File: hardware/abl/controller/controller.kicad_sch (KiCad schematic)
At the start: 31 parts, among them IC1 LSF0204PWJ, IC2 FXL6408UMX, IC3 VEML6040A3OG, IC4 FXL6408UMX, J1 SFW20S-2STE1LF, J2 Conn_02x03_Odd_Even, J3 Conn_02x03_Odd_Even, J4 PRT-14417, J5 Conn_02x04_Odd_Even, Q2 AO3401A, Q4 AO3401A, U1 INA219AxD

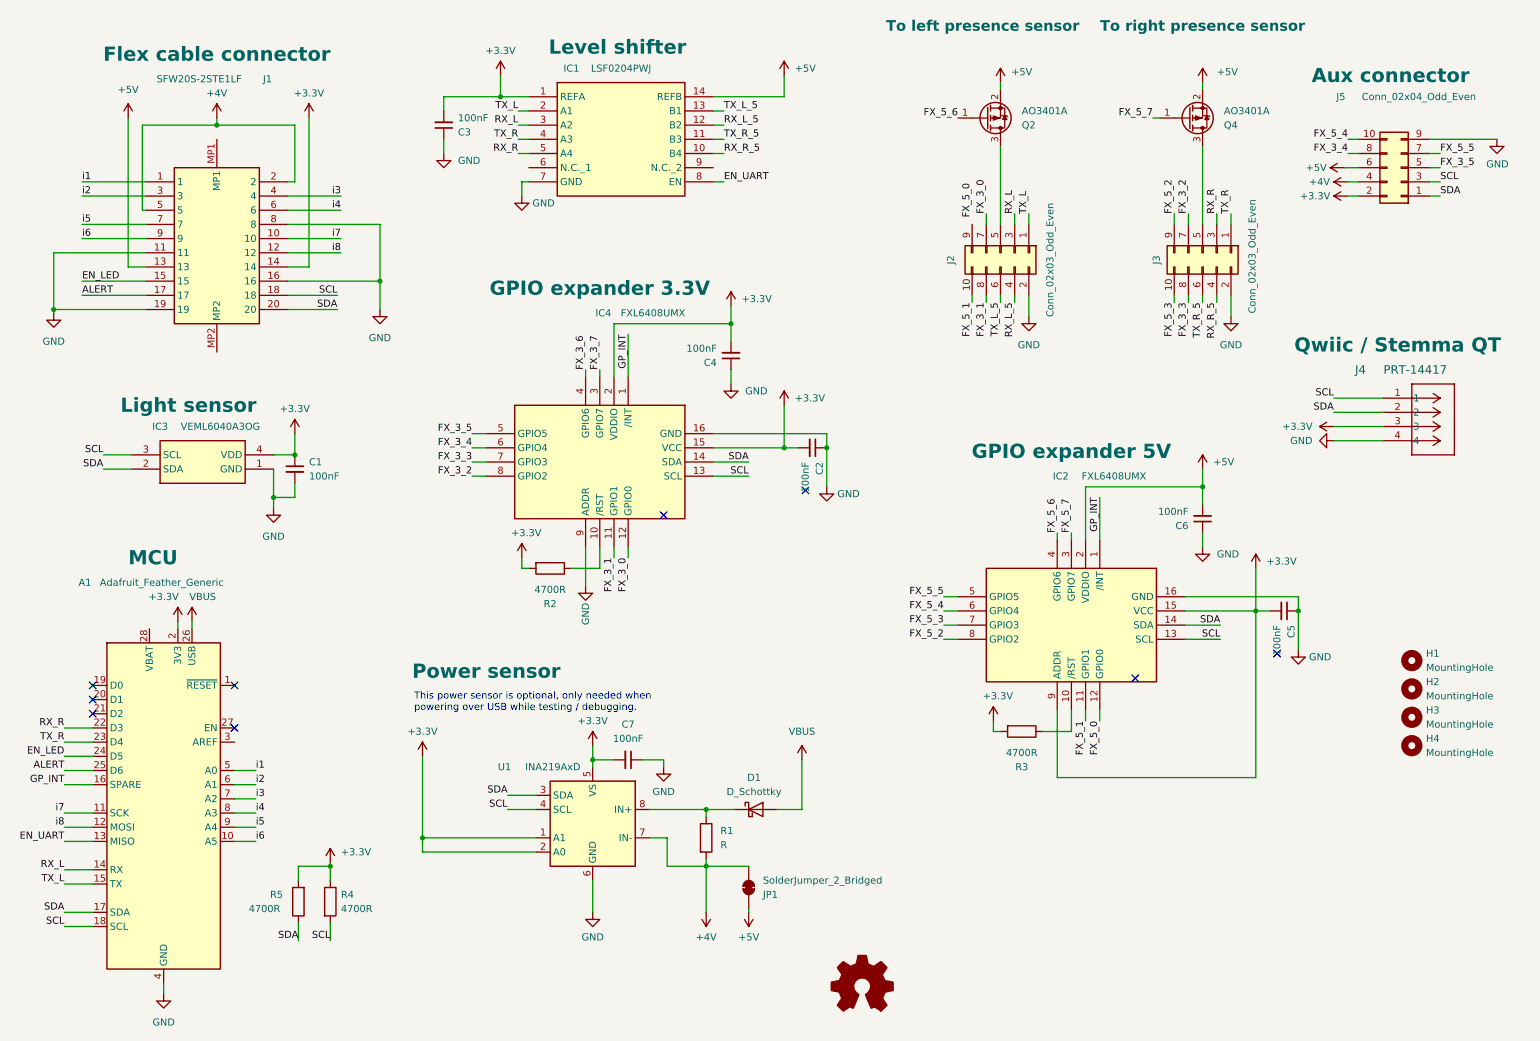
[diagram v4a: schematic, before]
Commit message: Make controller PCB ready for prototype prodution: change level shifter, re-route many traces, etc.
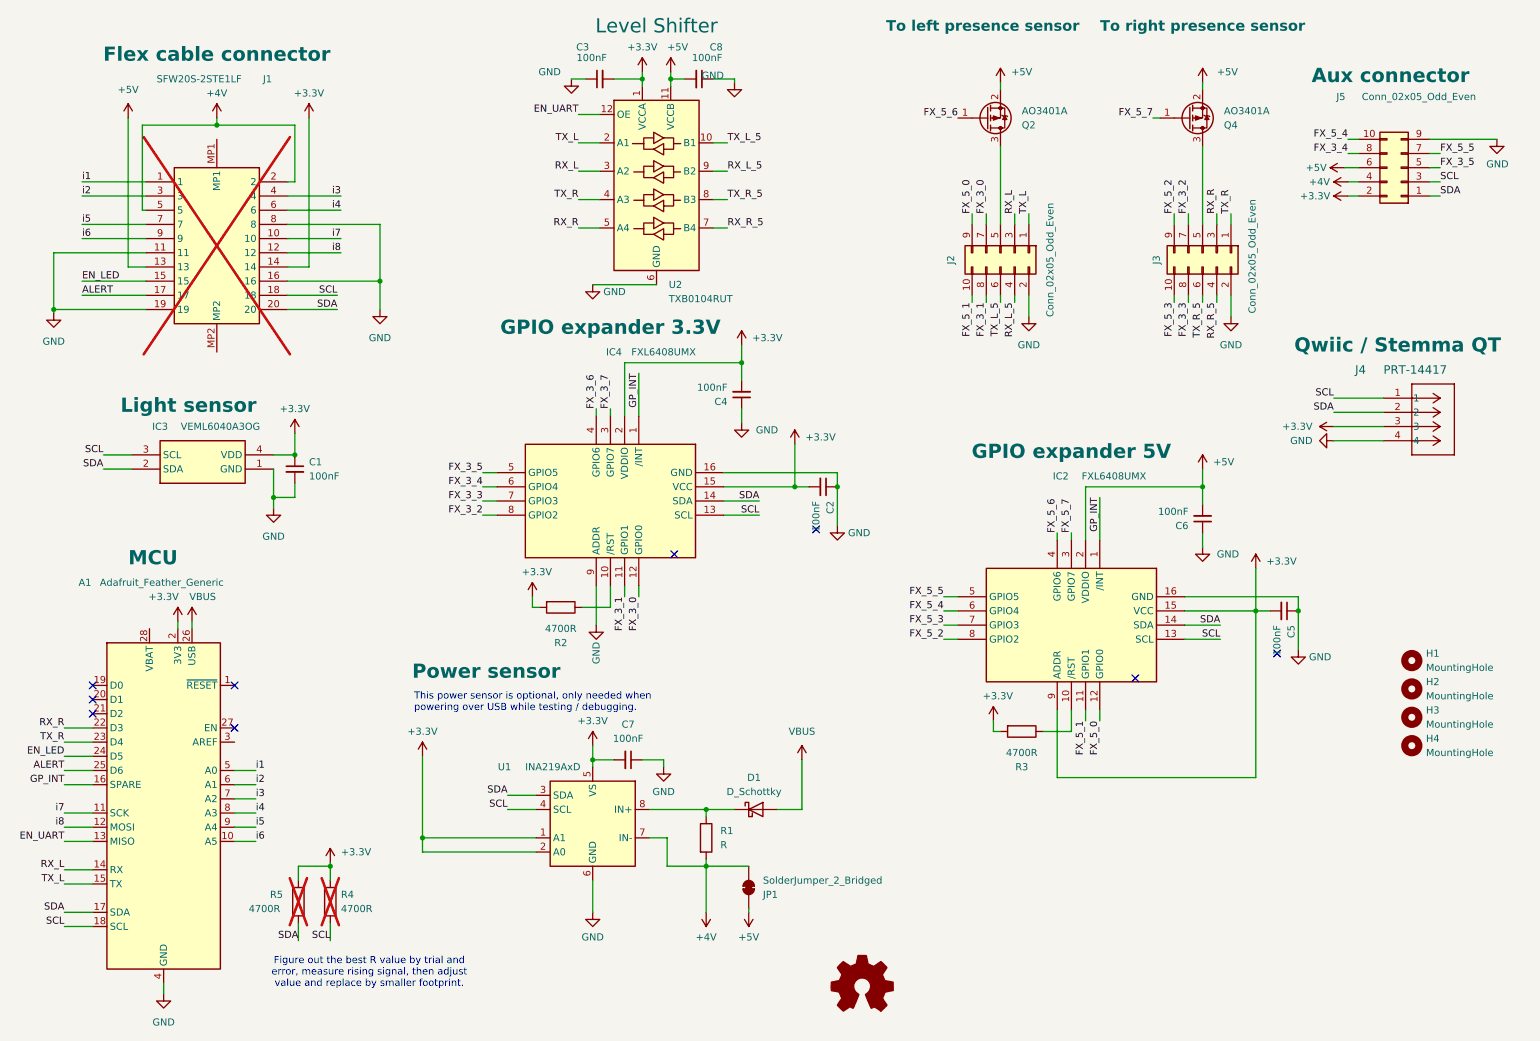
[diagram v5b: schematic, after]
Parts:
- removed IC1: LSF0204PWJ, SOP65P640X110-14N, symbol LSF0204PWJ:LSF0204PWJ
- added C8: 100nF, Capacitor_SMD:C_0402_1005Metric, symbol Device:C_Small
- added U2: TXB0104RUT, Package_DFN_QFN:Texas_R-PUQFN-N12, symbol Logic_LevelTranslator:TXB0104RUT
- J1: now not fitted
- J2, J3: value Conn_02x03_Odd_Even -> Conn_02x05_Odd_Even; LCSC Part # (none) -> C7501276
- J5: value Conn_02x04_Odd_Even -> Conn_02x05_Odd_Even; LCSC Part # (none) -> C7501276
- R4, R5: footprint Resistor_SMD:R_0402_1005Metric -> Resistor_SMD:R_0805_2012Metric_Pad1.20x1.40mm_HandSolder; now not fitted
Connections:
- net +3.3V: now also U2.1 (VCCA)
- net +5V: now also C8.2, U2.11 (VCCB)
- net EN_UART: now also U2.12 (OE)
- net FX_5_0: now also J2.9 (Pin_9)
- net GND: now also C8.1, U2.6 (GND)
- net RX_L: now also U2.3 (A2)
- net RX_L_5: now also U2.9 (B2)
- net RX_R: now also U2.5 (A4)
- net RX_R_5: now also U2.7 (B4)
- net TX_L: now also U2.2 (A1)
- net TX_L_5: now also U2.10 (B1)
- net TX_R: now also U2.4 (A3)
- net TX_R_5: now also U2.8 (B3)
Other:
- note added: "Figure out the best R value by trial and error, measure rising signal, then adjust value and replace by smaller footprint."
- moved on the sheet: C2, C3, C4, IC4, R2

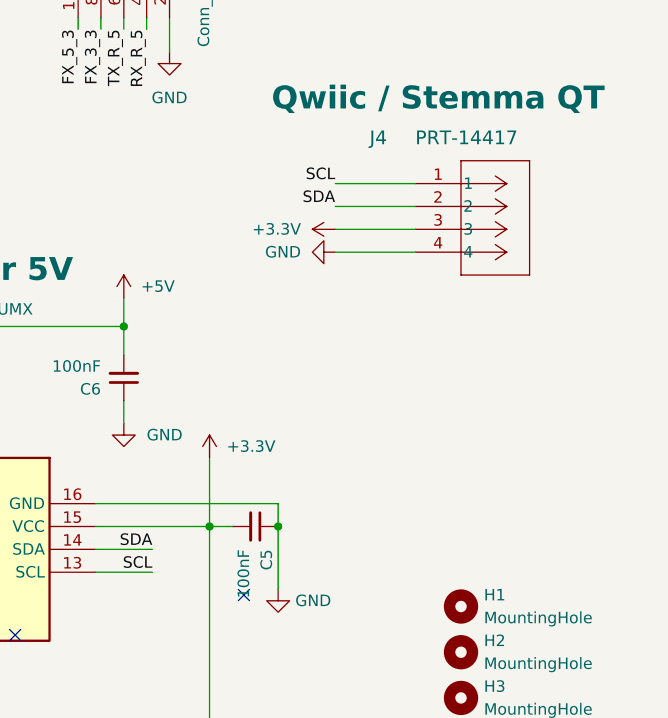
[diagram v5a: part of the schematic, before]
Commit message: Fix orientation of Stemma QT / Quiic socket, add test points for voltages.
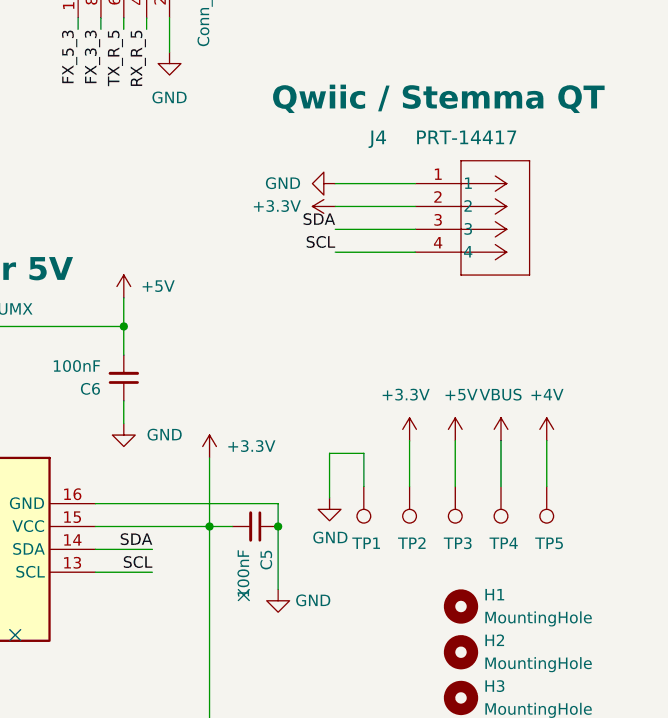
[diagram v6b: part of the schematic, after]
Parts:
- added TP1, TP2, TP3, TP4, TP5: TestPoint, TestPoint:TestPoint_THTPad_D1.5mm_Drill0.7mm, symbol Connector:TestPoint
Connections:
- net +3.3V: now also J4.2, TP2.1; no longer J4.3
- net +4V: now also TP5.1
- net +5V: now also TP3.1
- net GND: now also J4.1, TP1.1; no longer J4.4
- net SCL: now also J4.4; no longer J4.1
- net SDA: now also J4.3; no longer J4.2
- net VBUS: now also TP4.1

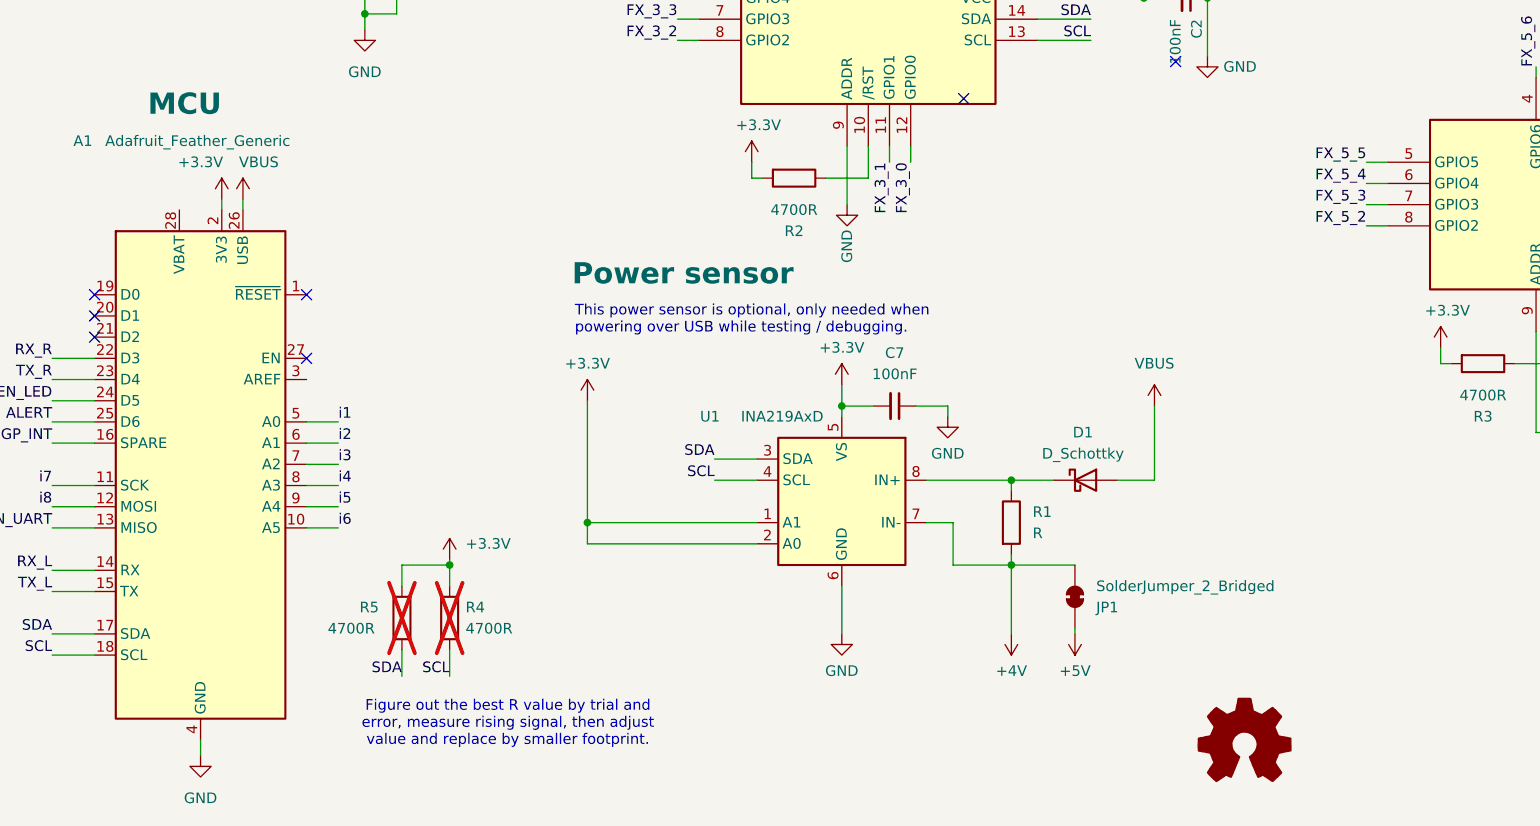
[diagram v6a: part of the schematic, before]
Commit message: Fix 5V power supply for Feather.
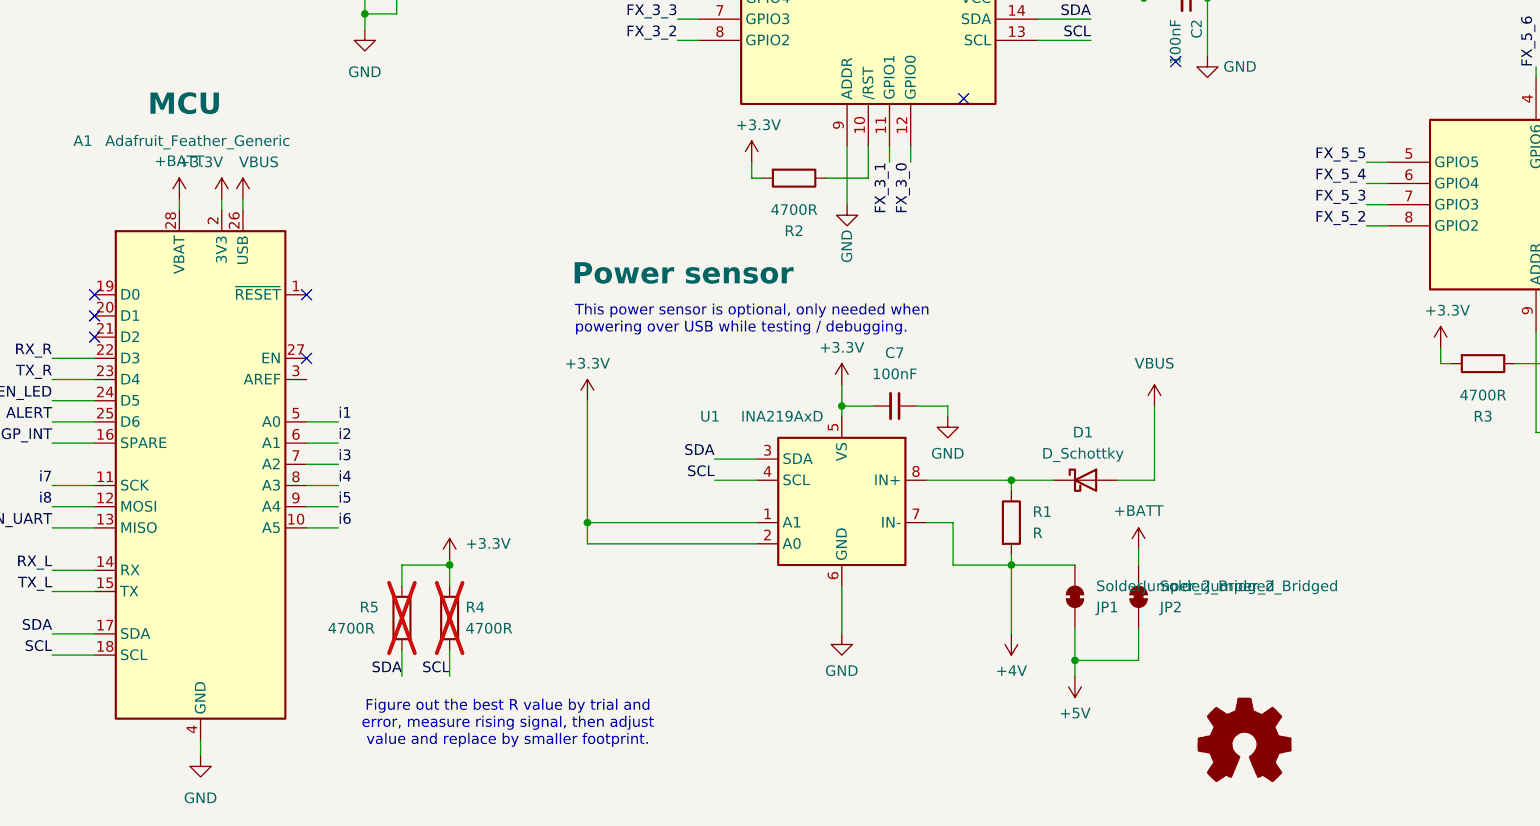
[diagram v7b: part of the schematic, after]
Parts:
- added JP2: SolderJumper_2_Bridged, Jumper:SolderJumper-2_P1.3mm_Bridged2Bar_RoundedPad1.0x1.5mm, symbol Jumper:SolderJumper_2_Bridged
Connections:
- net +5V: now also JP2.2 (B)
- net +BATT: now reaches A1.28 (VBAT)
- net +BATT: now also JP2.1 (A)
